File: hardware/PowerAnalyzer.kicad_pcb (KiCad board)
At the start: 2 copper layers, 55.9 x 45.7 mm, 59 parts, among them J1 EXPANSION, J10 TEST_IN, J11 PWR_IN, J12 PWR_OUT, J2 UDPI, J3 I2C, J4 FAN, J5 NTC, J6 UART, J7 USB_C_Receptacle_USB2.0_16P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

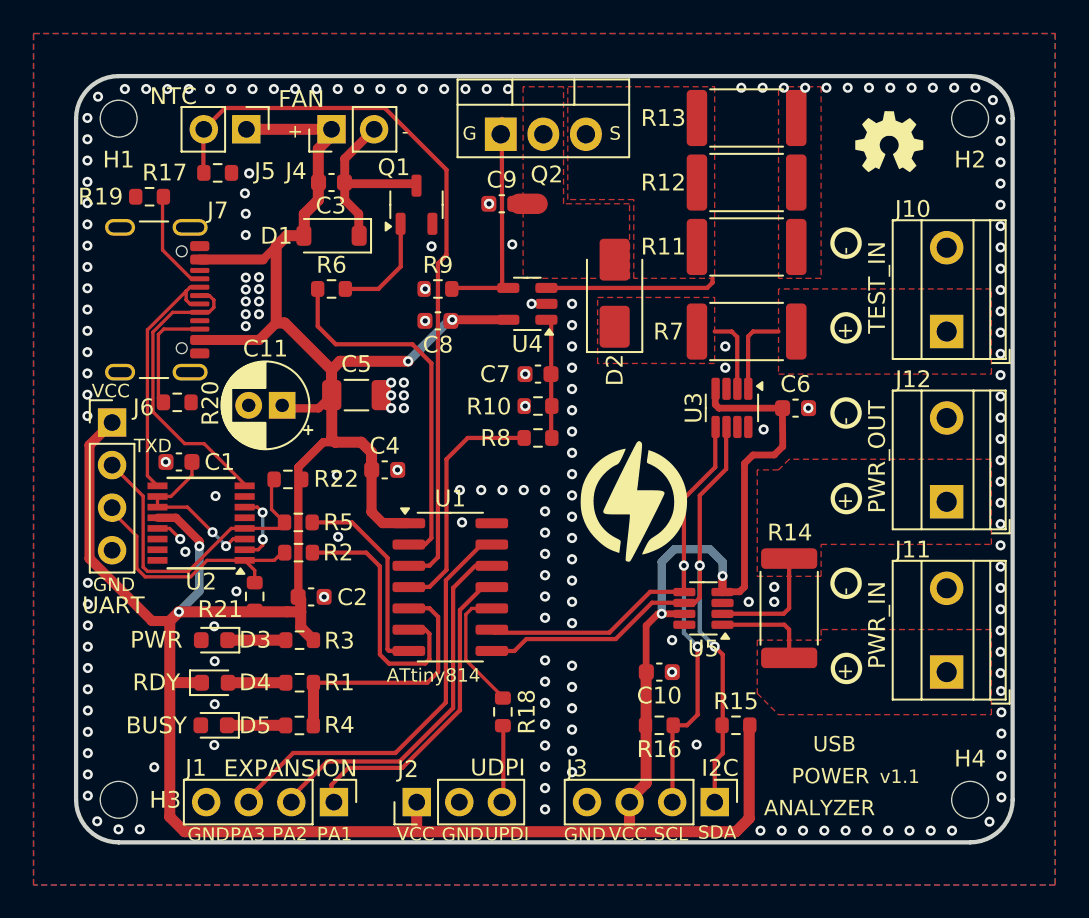
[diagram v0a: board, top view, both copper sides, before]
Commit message: Fix diodes
Their pins are numbered differently on easyEDA.
Move some vias which may cause tombstoning.
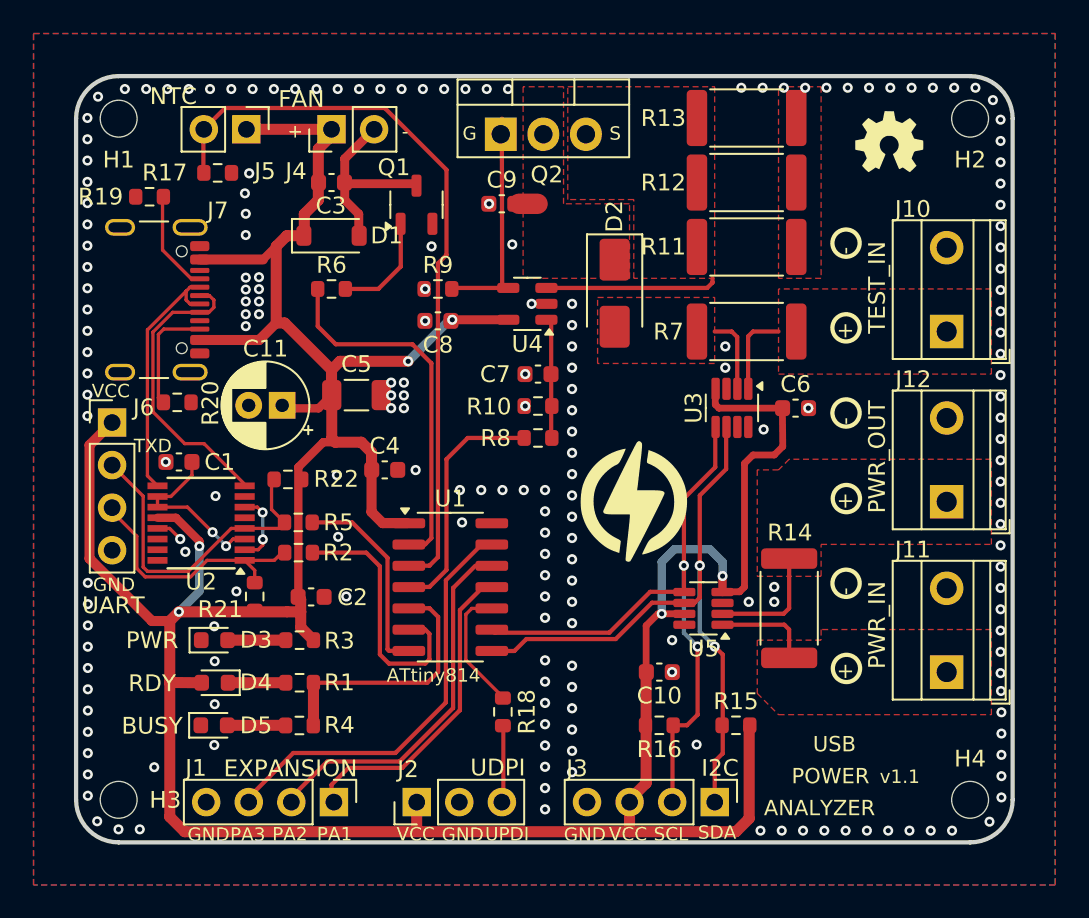
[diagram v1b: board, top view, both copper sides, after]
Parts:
- turned D1 to 0 degrees
- turned D2 to -90 degrees
- turned D3 to 0 degrees
- turned D4 to 180 degrees
- turned D5 to 0 degrees
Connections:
- D1 pad 1: FAN- -> +5V
- D1 pad 2: +5V -> FAN-
- D2 pad 1: TEST -> Net-(D2-K)
- D2 pad 2: Net-(D2-K) -> TEST
- D3 pad 1: Net-(D3-+) -> GND
- D3 pad 2: GND -> Net-(D3-A)
- D4 pad 1: +5V -> Net-(D4-K)
- D4 pad 2: Net-(D4--) -> +5V
- D5 pad 1: Net-(D5-+) -> GND
- D5 pad 2: GND -> Net-(D5-A)
- R1 pad 2: Net-(D4--) -> Net-(D4-K)
- R3 pad 2: Net-(D3-+) -> Net-(D3-A)
- R4 pad 2: Net-(D5-+) -> Net-(D5-A)
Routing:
- net Net-(D5-A): track 0.00 -> 3.49 mm
- net Net-(D5-+): track 3.49 -> 0.00 mm
- net Net-(D3-A): track 0.00 -> 3.47 mm
- net Net-(D3-+): track 3.47 -> 0.00 mm
- net Net-(D4-K): track 0.00 -> 3.44 mm
- net Net-(D4--): track 3.44 -> 0.00 mm

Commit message: Pocket Power Prowler v2
Migrate from semi-constant current control via shunt and operational
amplifier to direct DAC- and P[ID]-based control algorithm.
Bias the op amp just below the MOSFET threshold voltage to make use of
full DAC range.
Reduce DAC output capacitance from 100 n to 10 p (in order to filter out
high frequencies coming from DAC peripheral clock).

Shield the op amp and the fan controller.

Allow for powering the fan with external power.

Remove the series diode with the load, unsure for the reason of its
existance, but no literature seems to confirm the need for it.

Make the board a tad smaller.
Rebrand!
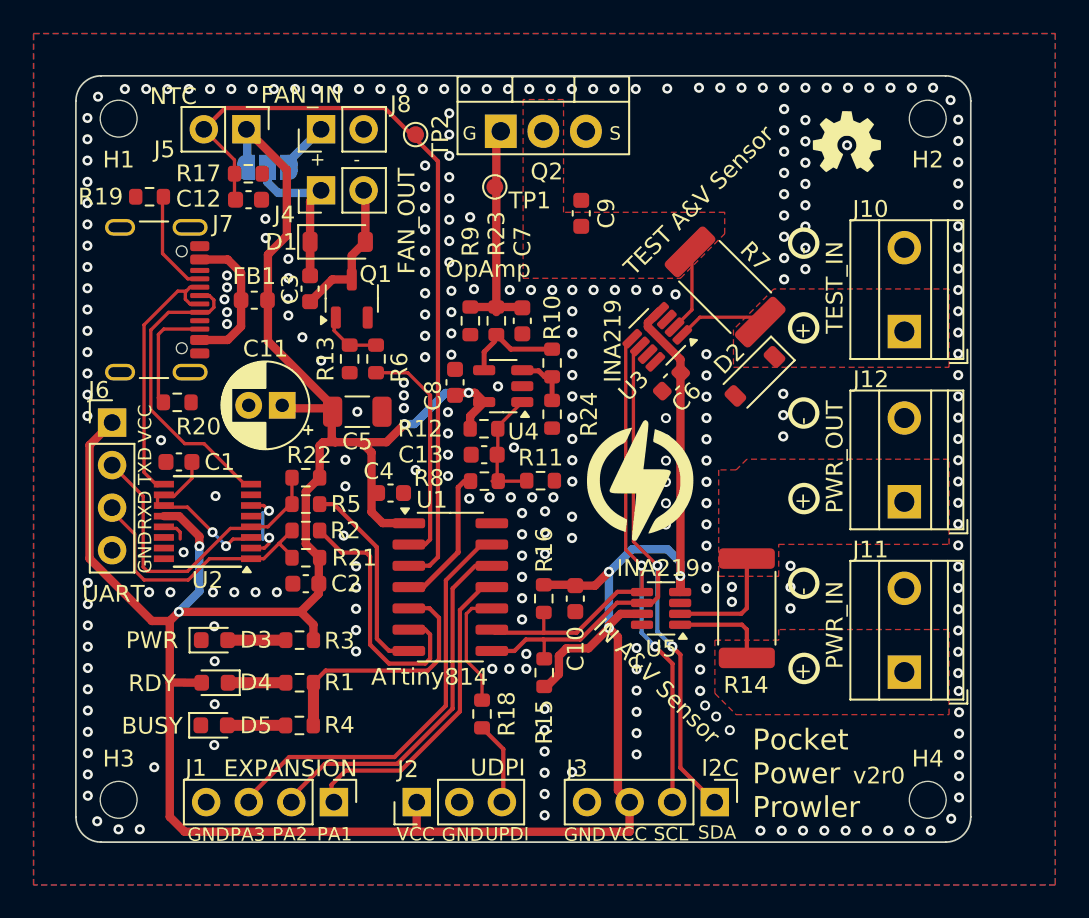
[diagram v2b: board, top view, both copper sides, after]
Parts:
- added C12: 100n, Capacitor_SMD:C_0603_1608Metric, F.Cu at (130.3, 87.4)
- added C13: 10p, Capacitor_SMD:C_0603_1608Metric, F.Cu at (144.3, 102.6)
- added FB1: FerriteBead, Inductor_SMD:L_0603_1608Metric, F.Cu at (130.6, 93.4)
- added J8: FAN_IN, Connector_PinHeader_2.54mm:PinHeader_1x02_P2.54mm_Vertical, F.Cu at (134.6, 83.2)
- added JP1: SolderJumper_3_Open, Jumper:SolderJumper-3_P1.3mm_Open_RoundedPad1.0x1.5mm, B.Cu at (131.4, 85.4)
- added R23: 47, Resistor_SMD:R_0603_1608Metric, F.Cu at (145.1, 94.6)
- added R24: 22k, Resistor_SMD:R_0603_1608Metric, F.Cu at (148.4, 100.2)
- added TP1: GATE, TestPoint:TestPoint_Pad_D1.0mm, F.Cu at (145.0, 86.6)
- added TP2: NTC, TestPoint:TestPoint_Pad_D1.0mm, F.Cu at (140.3, 83.5)
- C3: value 100n -> 1u
- C7: value 100n -> 4.7n
- D2: value SS54 -> 1N4148W; footprint Diode_SMD:D_SMA -> Diode_SMD:D_SOD-123
- J4: value FAN -> FAN_OUT
- R10: value 1k5 -> 10k
- R11: value 300m -> 6.8k; footprint Resistor_SMD:R_2512_6332Metric -> Resistor_SMD:R_0603_1608Metric
- R12, R13: value 300m -> 10k; footprint Resistor_SMD:R_2512_6332Metric -> Resistor_SMD:R_0603_1608Metric
- R8: value 10k -> 5.1k
- moved R13 27.7 mm to (136.3, 96.9), turned to 90 degrees
- moved R12 21.5 mm to (144.3, 101.0)
- moved R11 18.6 mm to (147.7, 104.1)
- moved R15 11.9 mm to (147.9, 115.6), turned to 90 degrees
- moved R16 10.2 mm to (147.9, 111.2), turned to -90 degrees
- moved D2 9.73 mm to (160.5, 97.9), turned to -135 degrees
- moved C6 7.57 mm to (155.5, 98.2), turned to -135 degrees
- moved Q1 6.80 mm to (136.4, 93.3)
- moved C10 6.66 mm to (149.8, 111.2), turned to -90 degrees
- moved C3 6.46 mm to (134.0, 92.7), turned to -90 degrees
- moved U3 6.15 mm to (154.7, 95.6), turned to -135 degrees
- moved U4 5.12 mm to (145.5, 98.5)
- moved R6 4.95 mm to (137.9, 96.9), turned to 90 degrees
- moved C9 4.77 mm to (150.1, 88.2), turned to 90 degrees
- moved R8 4.11 mm to (144.4, 104.2), turned to 0 degrees
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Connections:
- net FAN renamed FAN_EN
- C3 pad 1: +5V -> FAN_OUT
- C7 pad 1: Net-(U4-IN+) -> GATE
- C9 pad 1: GND -> TEST
- C9 pad 2: Net-(D2-K) -> GND
- D1 pad 1: +5V -> FAN_OUT
- D2 pad 1: Net-(D2-K) -> TEST_IN
- D2 pad 2: TEST -> GND
- J4 pad 1: +5V -> FAN_OUT
- J7 pad A4: +5V -> VBUS
- J7 pad A9: +5V -> VBUS
- J7 pad B4: +5V -> VBUS
- J7 pad B9: +5V -> VBUS
- Q2 pad 2: Net-(D2-K) -> TEST
- Q2 pad 3: SHUNT -> GND
- R10 pad 1: GND -> Net-(U4--)
- R10 pad 2: Net-(U4-IN+) -> Net-(R10-Pad2)
- R11 pad 2: SHUNT -> Net-(U4-+)
- R12 pad 1: GND -> Net-(U4-+)
- R12 pad 2: SHUNT -> +5V
- R13 pad 2: SHUNT -> Net-(Q1-G)
- R15 pad 1: SDA -> +5V
- R15 pad 2: +5V -> SDA
- R16 pad 1: SCL -> +5V
- R16 pad 2: +5V -> SCL
- R21 pad 1: +5V -> RXD
- R21 pad 2: RXD -> +5V
- R22 pad 1: +5V -> TXD
- R22 pad 2: TXD -> +5V
- R8 pad 1: Net-(U4-IN+) -> DAC
- R8 pad 2: DAC -> Net-(U4-+)
- R9 pad 1: GND -> GATE
- R9 pad 2: GATE -> GND
- U4 pad 1: Net-(U4-IN+) -> Net-(U4-+)
- U4 pad 3: SHUNT -> Net-(U4--)
- U4 pad 4: GATE -> Net-(R10-Pad2)
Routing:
- net +5V: track 203.3 -> 187.2 mm, vias 6 -> 7
- net FAN_OUT: track 0.00 -> 11.3 mm
- net SHUNT: track 9.93 -> 0.00 mm
- net VBUS: track 0.00 -> 8.80 mm
- net FAN_EN: track 21.9 -> 13.9 mm
- net Net-(U4-+): track 0.00 -> 7.24 mm
- net Net-(U4-IN+): track 6.97 -> 0.00 mm
- net DAC: track 14.6 -> 8.29 mm
- net Net-(R10-Pad2): track 0.00 -> 5.66 mm
- net SDA: track 39.2 -> 43.1 mm
- net Net-(U4--): track 0.00 -> 3.30 mm
- net FAN_IN: track 0.00 -> 3.18 mm
- net SCL: track 38.5 -> 41.6 mm
- net FAN-: track 11.6 -> 8.58 mm
- net Net-(Q1-G): track 6.40 -> 3.47 mm
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- removed copper zone on F.Cu, net Net-(D2-K)
- removed copper zone on F.Cu, net SHUNT
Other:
- board size 55.9 x 45.7 mm -> 53.4 x 45.7 mm
- board text added: "1"
- board text added: "2"
- board text added: "3"
- board text added: "Fan power: 1-2: FAN_IN 2-3: 5 V"
- board text added: "IN A&V Sensor"
- board text added: "OpAmp"
- board text added: "Pocket Power Prowler"
- board text added: "RXD"
- board text added: "TEST A&V Sensor"
- board text added: "based on ATtiny814 Power Analyzer by Stefan Wagner"
- board text added: "by Maciej Małecki (mmalecki.com)"
- board text added: "github.com/mmalecki/pocket-power-prowler"
- board text added: "v2r0"
- board text removed: "2020 by Stefan Wagner"
- board text removed: "ANALYZER"
- board text removed: "POWER"
- board text removed: "USB"
- board text removed: "USB POWER ANALYZER"
- board text removed: "refreshed in 2024 by Maciej Małecki"
- board text removed: "v1.1"

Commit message: Finish (?) KiCadifying
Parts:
- turned R1 to 0 degrees
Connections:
- R1 pad 1: LED -> Net-(D4-K)
- R1 pad 2: Net-(D4-K) -> LED

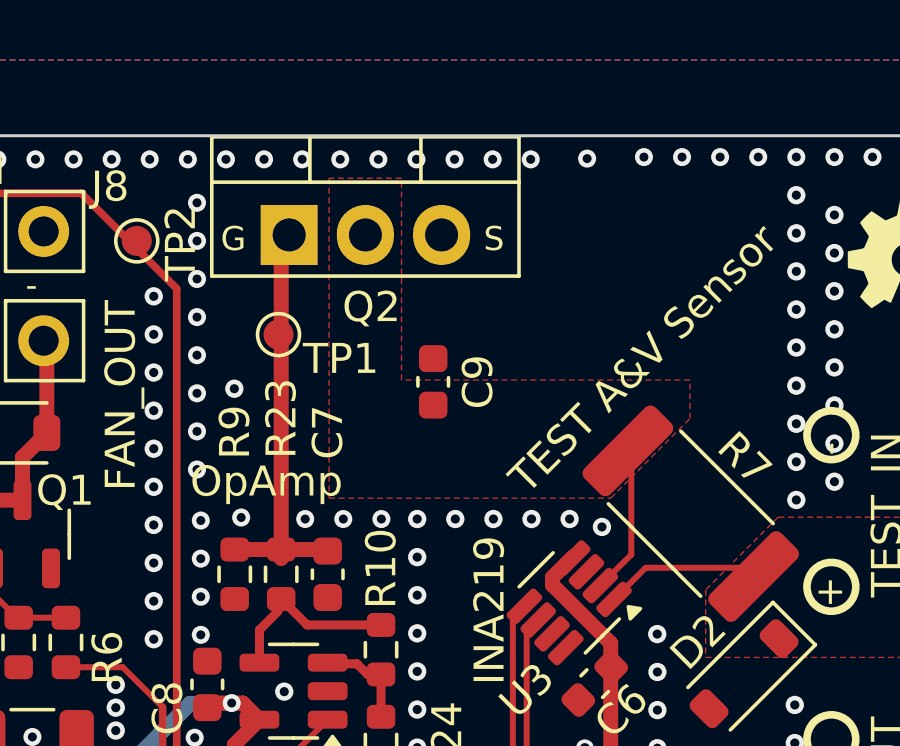
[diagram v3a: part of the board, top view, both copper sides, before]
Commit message: Move the transistor a bit to the right
Allow more space for the heatsink.
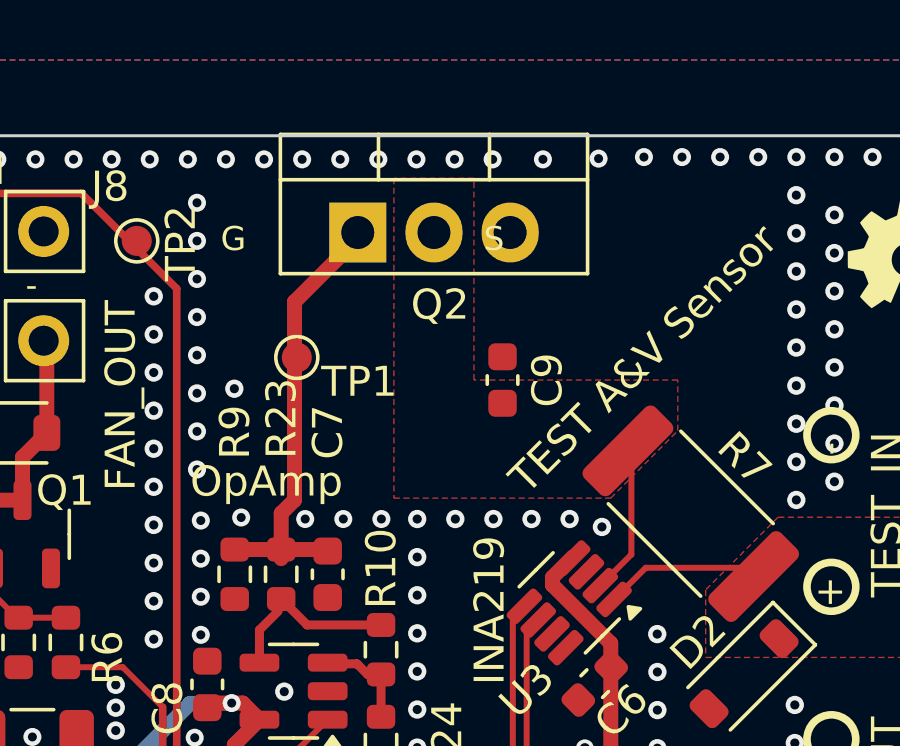
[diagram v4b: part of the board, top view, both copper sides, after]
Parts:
- moved C9 2.31 mm to (152.5, 88.1)
- moved Q2 2.29 mm to (147.6, 83.2)
- moved TP1 0.98 mm to (145.6, 87.4)
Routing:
- net GATE: track 13.9 -> 15.0 mm
